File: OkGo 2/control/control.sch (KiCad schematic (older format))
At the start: 36 parts

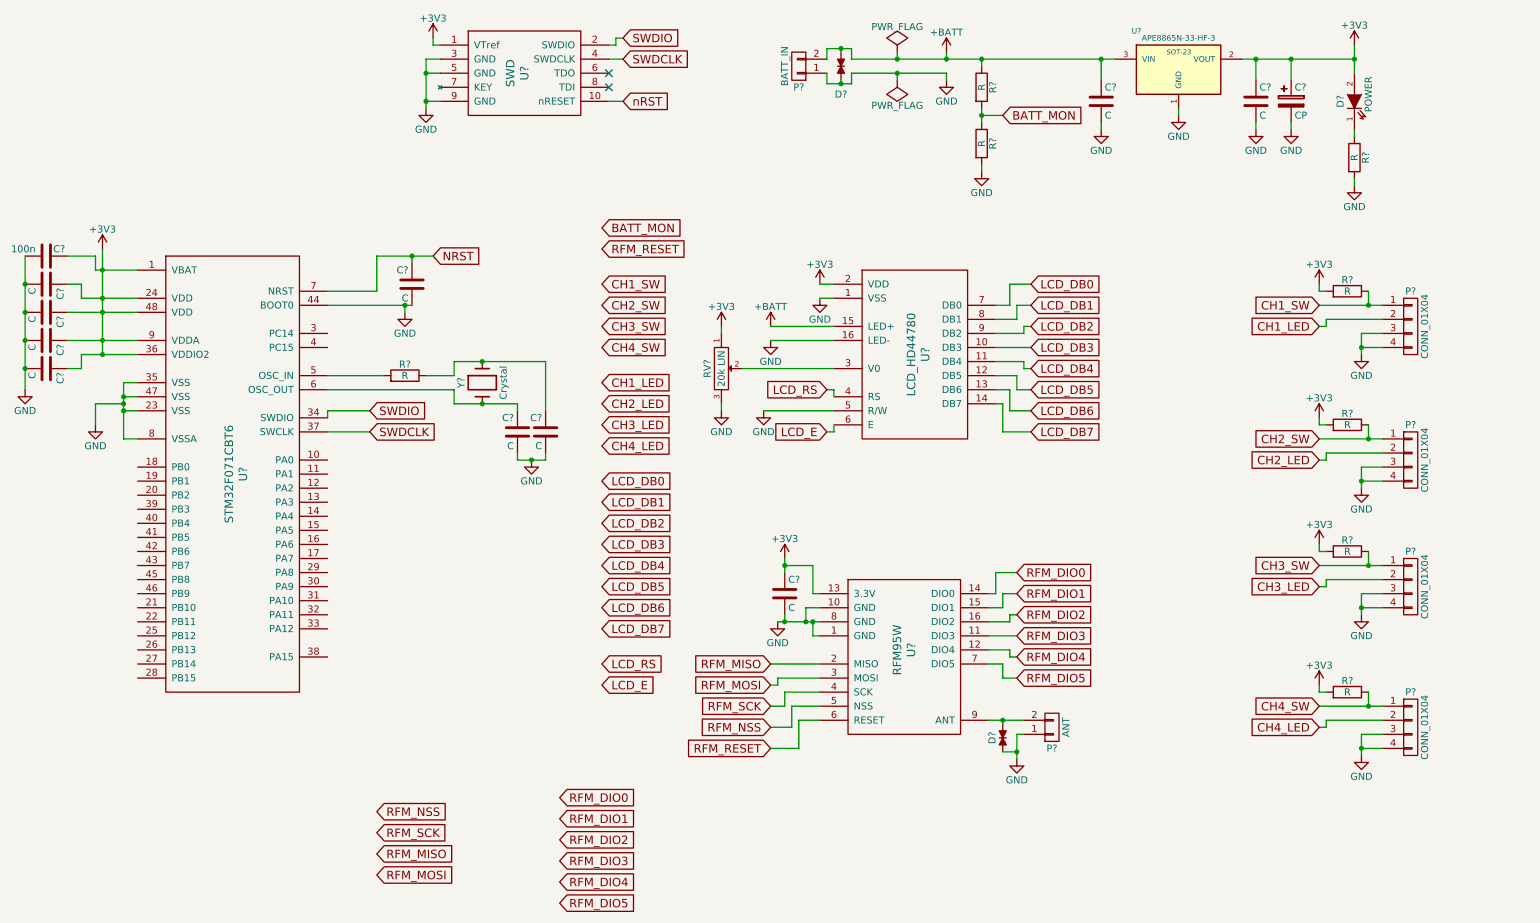
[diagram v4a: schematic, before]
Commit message: Upstream relay, hierarchical sheets, local labels
* Added upstream failsafe relay and stuck relay sensing
* Moved out firing circuits to a separate sub-sheet below control
* Converted all global labels to local labels
* Fixed typo in naming of nRST on control sheet

Resolves #12.
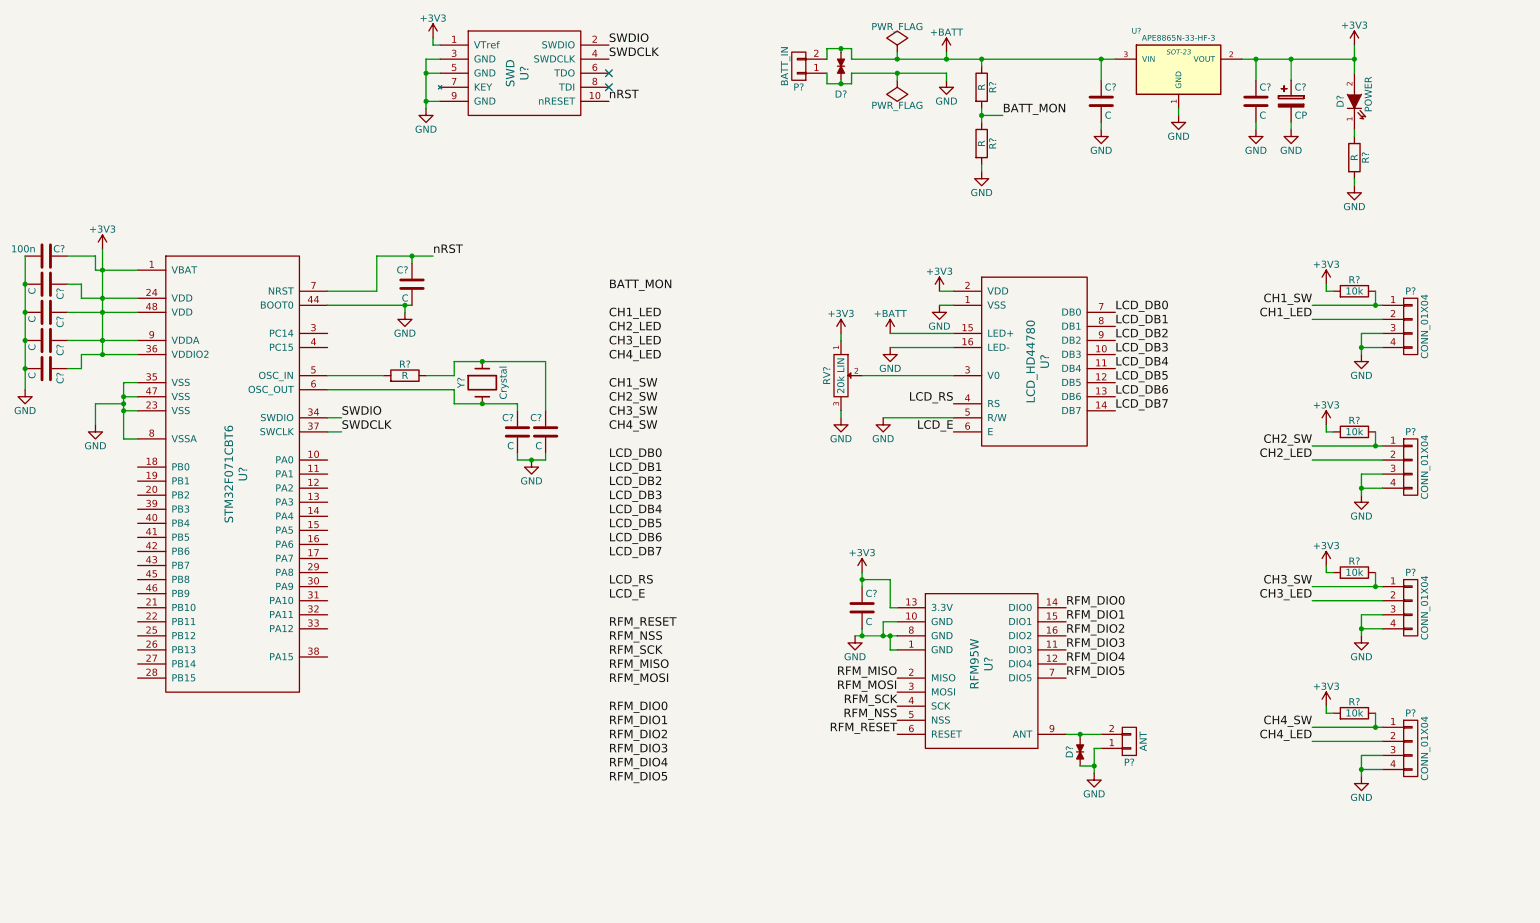
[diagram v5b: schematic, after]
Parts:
- removed P? (x3): CONN_01X04, symbol CONN_01X04
- removed R? (x3): R, symbol R
- added P? (x3): CONN_01X04, symbol CONN_01X04
- added R? (x3): 10k, symbol R
- R?: value R -> 10k
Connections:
- net NRST is gone; now on net nRST: C?.1, U?.7 (NRST)
- net +3V3: now also R?.2, R?.2, R?.2
- net CH2_LED: now also P?.2 (P2)
- net CH2_SW: now also P?.1 (P1), R?.1
- net CH3_LED: now also P?.2 (P2)
- net CH3_SW: now also P?.1 (P1), R?.1
- net CH4_LED: now also P?.2 (P2)
- net CH4_SW: now also P?.1 (P1), R?.1
- net GND: now also P?.3 (P3), P?.3 (P3), P?.3 (P3), P?.4 (P4), P?.4 (P4), P?.4 (P4)
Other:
- moved on the sheet: C?, D?, P?, R?, RV?, U?

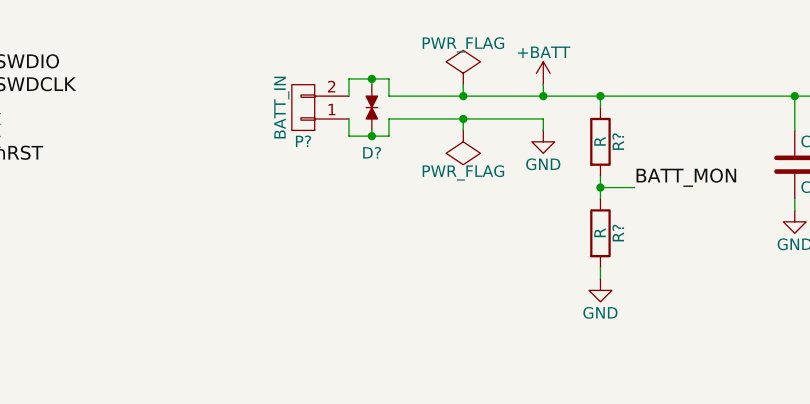
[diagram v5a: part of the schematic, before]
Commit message: Removed pin labels from TVS
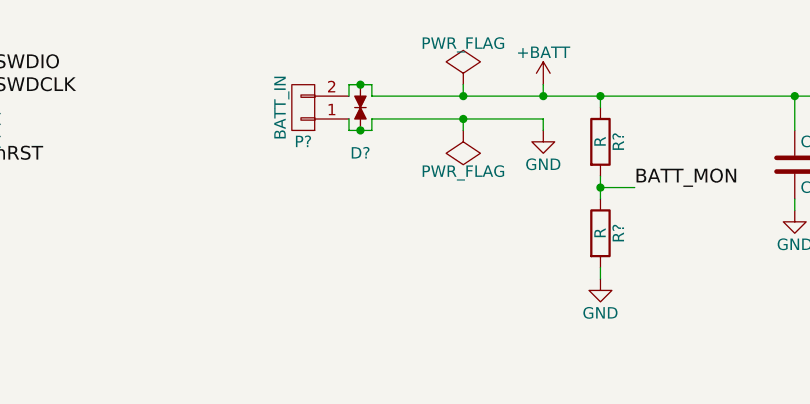
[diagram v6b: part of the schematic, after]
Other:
- moved on the sheet: D?
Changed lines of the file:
@@
 Connection ~ 9850 1100
 Wire Wire Line
-	6725 1200 7050 1200
+	6650 1200 7050 1200
 Wire Wire Line
 	7050 1200 7400 1200
@@
 Connection ~ 7650 1500
 Wire Wire Line
-	6725 1100 7050 1100
+	6650 1100 7050 1100
 Wire Wire Line
 	7050 1100 7400 1100
@@
 L TVS_small D?
 U 1 1 559DC9F3
-P 6650 1150
-F 0 "D?" V 6850 1150 50  0000 C CNN
-F 1 "TVS_small" H 6650 1075 50  0001 C CNN
-F 2 "Resistors_SMD:R_0603_HandSoldering" H 6650 1150 60  0001 C CNN
-F 3 "" H 6650 1150 60  0000 C CNN
-F 4 "2368174" H 6650 1150 60  0001 C CNN "Farnell"
-	1    6650 1150
+P 6600 1150
+F 0 "D?" V 6800 1150 50  0000 C CNN
+F 1 "TVS_small" H 6600 1075 50  0001 C CNN
+F 2 "Resistors_SMD:R_0603_HandSoldering" H 6600 1150 60  0001 C CNN
+F 3 "" H 6600 1150 60  0000 C CNN
+F 4 "2368174" H 6600 1150 60  0001 C CNN "Farnell"
+	1    6600 1150
 	0    1    1    0
 $EndComp
 Wire Wire Line
-	6550 1100 6550 1025
-Wire Wire Line
-	6550 1025 6650 1025
-Wire Wire Line
-	6650 1025 6725 1025
-Wire Wire Line
-	6650 1025 6650 1050
-Wire Wire Line
-	6725 1025 6725 1100
-Connection ~ 6650 1025
-Wire Wire Line
-	6550 1200 6550 1275
-Wire Wire Line
-	6550 1275 6650 1275
-Wire Wire Line
-	6650 1275 6725 1275
-Wire Wire Line
-	6650 1275 6650 1250
-Wire Wire Line
-	6725 1275 6725 1200
-Connection ~ 6650 1275
+	6550 1100 6550 1050
+Wire Wire Line
+	6550 1050 6600 1050
+Wire Wire Line
+	6600 1050 6650 1050
+Wire Wire Line
+	6600 1050 6600 1050
+Wire Wire Line
+	6650 1050 6650 1100
+Connection ~ 6600 1050
+Wire Wire Line
+	6550 1200 6550 1250
+Wire Wire Line
+	6550 1250 6600 1250
+Wire Wire Line
+	6600 1250 6650 1250
+Wire Wire Line
+	6600 1250 6600 1250
+Wire Wire Line
+	6650 1250 6650 1200
+Connection ~ 6600 1250
 Connection ~ 7650 1100
 $Comp

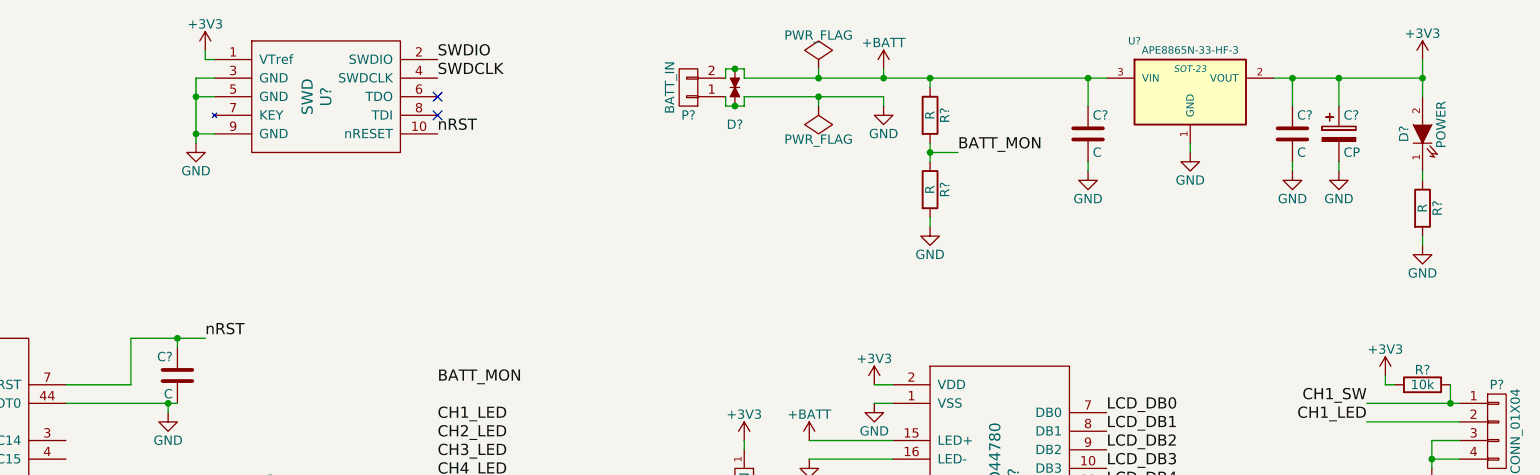
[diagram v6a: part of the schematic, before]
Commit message: Test points. Resolves #14
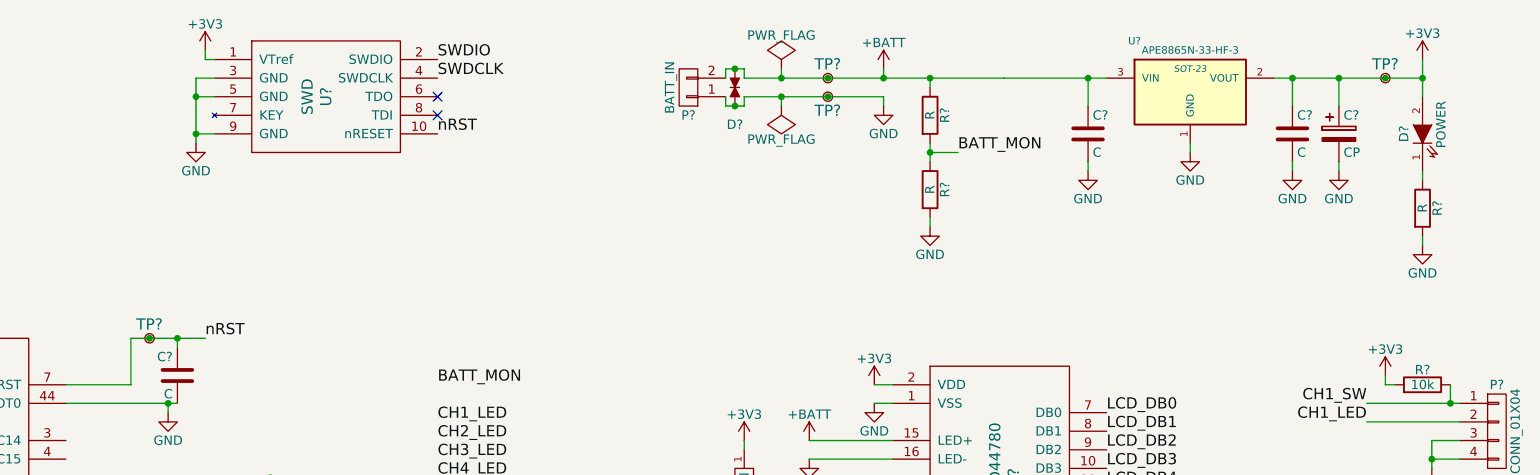
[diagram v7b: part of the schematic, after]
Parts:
- added TP? (x4): TestPoint, symbol TestPoint
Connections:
- net +3V3: now also TP?.1
- net +BATT: now also TP?.1
- net GND: now also TP?.1
- net nRST: now also TP?.1
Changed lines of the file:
@@
 LIBS:stm32f071cbt6
 LIBS:tvs_small
+LIBS:testpoint
 LIBS:control-cache
 EELAYER 25 0
@@
 L PWR_FLAG #FLG?
 U 1 1 556217FC
-P 7050 1050
-F 0 "#FLG?" H 7050 1145 50  0001 C CNN
-F 1 "PWR_FLAG" H 7050 1230 50  0000 C CNN
-F 2 "" H 7050 1050 60  0000 C CNN
-F 3 "" H 7050 1050 60  0000 C CNN
-	1    7050 1050
+P 6850 1050
+F 0 "#FLG?" H 6850 1145 50  0001 C CNN
+F 1 "PWR_FLAG" H 6850 1230 50  0000 C CNN
+F 2 "" H 6850 1050 60  0000 C CNN
+F 3 "" H 6850 1050 60  0000 C CNN
+	1    6850 1050
 	1    0    0    -1
 $EndComp
@@
 L PWR_FLAG #FLG?
 U 1 1 55621881
-P 7050 1250
-F 0 "#FLG?" H 7050 1345 50  0001 C CNN
-F 1 "PWR_FLAG" H 7050 1430 50  0000 C CNN
-F 2 "" H 7050 1250 60  0000 C CNN
-F 3 "" H 7050 1250 60  0000 C CNN
-	1    7050 1250
+P 6850 1250
+F 0 "#FLG?" H 6850 1345 50  0001 C CNN
+F 1 "PWR_FLAG" H 6850 1430 50  0000 C CNN
+F 2 "" H 6850 1250 60  0000 C CNN
+F 3 "" H 6850 1250 60  0000 C CNN
+	1    6850 1250
 	-1   0    0    1
 $EndComp
@@
 	9600 1100 9850 1100
 Wire Wire Line
-	9850 1100 10300 1100
+	9850 1100 10100 1100
+Wire Wire Line
+	10100 1100 10300 1100
 Wire Wire Line
 	9600 1100 9600 1250
@@
 Connection ~ 9850 1100
 Wire Wire Line
-	6650 1200 7050 1200
-Wire Wire Line
-	7050 1200 7400 1200
-Wire Wire Line
-	7050 1050 7050 1100
-Connection ~ 7050 1100
-Wire Wire Line
-	7050 1250 7050 1200
-Connection ~ 7050 1200
+	6650 1200 6850 1200
+Wire Wire Line
+	6850 1200 7400 1200
+Wire Wire Line
+	6850 1050 6850 1100
+Connection ~ 6850 1100
+Wire Wire Line
+	6850 1250 6850 1200
+Connection ~ 6850 1200
 Wire Wire Line
 	7400 1100 7400 1050
@@
 Connection ~ 7650 1500
 Wire Wire Line
-	6650 1100 7050 1100
-Wire Wire Line
-	7050 1100 7400 1100
+	6650 1100 6850 1100
+Wire Wire Line
+	6850 1100 7400 1100
 Wire Wire Line
 	7400 1100 7650 1100
 Wire Wire Line
-	7650 1100 8500 1100
+	7650 1100 8050 1100
+Wire Wire Line
+	8050 1100 8500 1100
 Wire Wire Line
 	8500 1100 8600 1100
@@
 Text Label 5000 2750 0    60   ~ 0
 BATT_MON
+$Comp
+L TestPoint TP?
+U 1 1 559DAAF9
+P 10100 1100
+F 0 "TP?" H 10100 1025 60  0000 C CNN
+F 1 "TestPoint" H 10075 925 60  0001 C CNN
+F 2 "" H 10100 1100 60  0000 C CNN
+F 3 "" H 10100 1100 60  0000 C CNN
+	1    10100 1100
+	-1   0    0    1
+$EndComp
+Connection ~ 10100 1100
+$Comp
+L TestPoint TP?
+U 1 1 559DAED6
+P 7100 1100
+F 0 "TP?" H 7100 1025 60  0000 C CNN
+F 1 "TestPoint" H 7075 925 60  0001 C CNN
+F 2 "" H 7100 1100 60  0000 C CNN
+F 3 "" H 7100 1100 60  0000 C CNN
+	1    7100 1100
+	-1   0    0    1
+$EndComp
+Connection ~ 7100 1100
+$Comp
+L TestPoint TP?
+U 1 1 559DAFE3
+P 7100 1200
+F 0 "TP?" H 7100 1125 60  0000 C CNN
+F 1 "TestPoint" H 7075 1025 60  0001 C CNN
+F 2 "" H 7100 1200 60  0000 C CNN
+F 3 "" H 7100 1200 60  0000 C CNN
+	1    7100 1200
+	1    0    0    -1
+$EndComp
+Connection ~ 7100 1200
+$Comp
+L TestPoint TP?
+U 1 1 559DB26A
+P 3450 2500
+F 0 "TP?" H 3450 2425 60  0000 C CNN
+F 1 "TestPoint" H 3425 2325 60  0001 C CNN
+F 2 "" H 3450 2500 60  0000 C CNN
+F 3 "" H 3450 2500 60  0000 C CNN
+	1    3450 2500
+	-1   0    0    1
+$EndComp
+Connection ~ 3450 2500
 $EndSCHEMATC
